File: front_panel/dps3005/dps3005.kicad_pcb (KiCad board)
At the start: 2 copper layers, 105.8 x 45.8 mm, 1 part

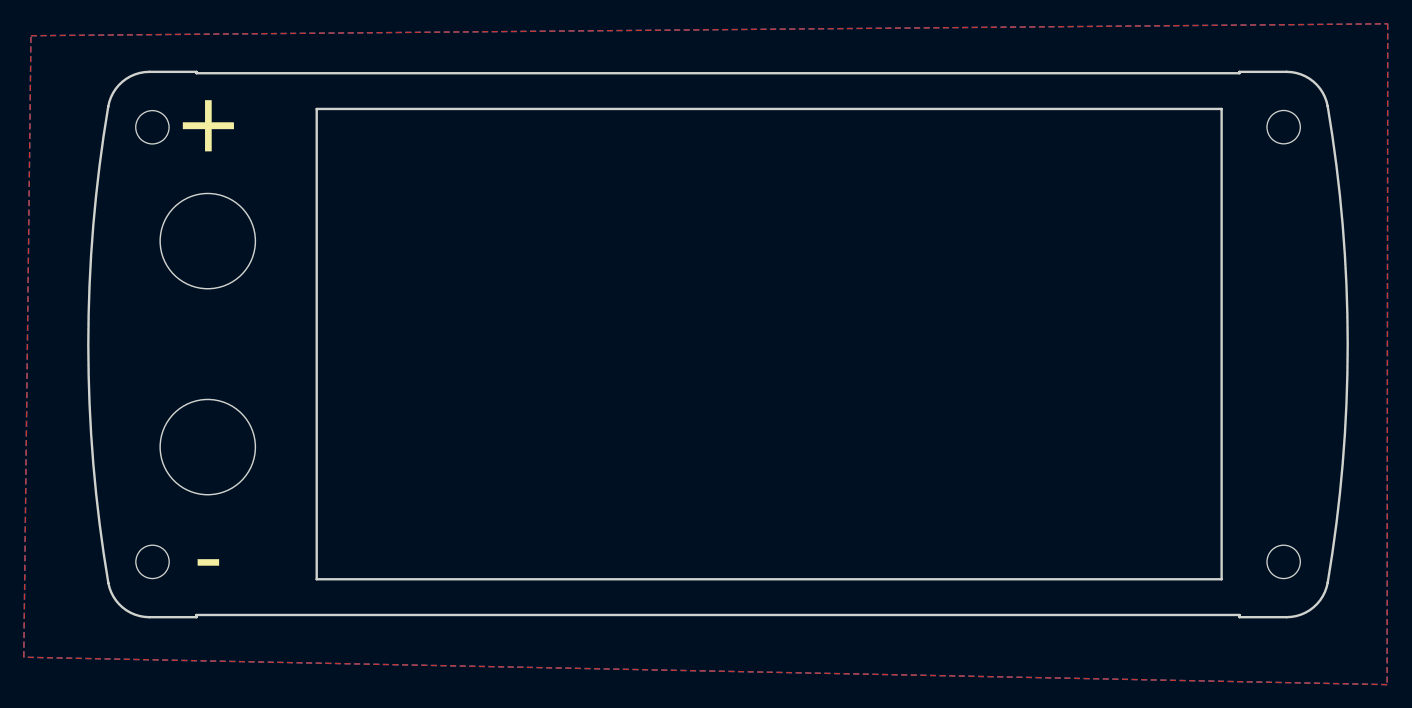
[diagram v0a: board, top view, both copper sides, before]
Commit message: Check failed again on JLCPCB because there was no drill file. All holes were made with the outline. Created a footprint for the binding posts and used KiCAD's 3mm mounting hole footprint for the screws. Sent back to JLCPCB for manufacture.
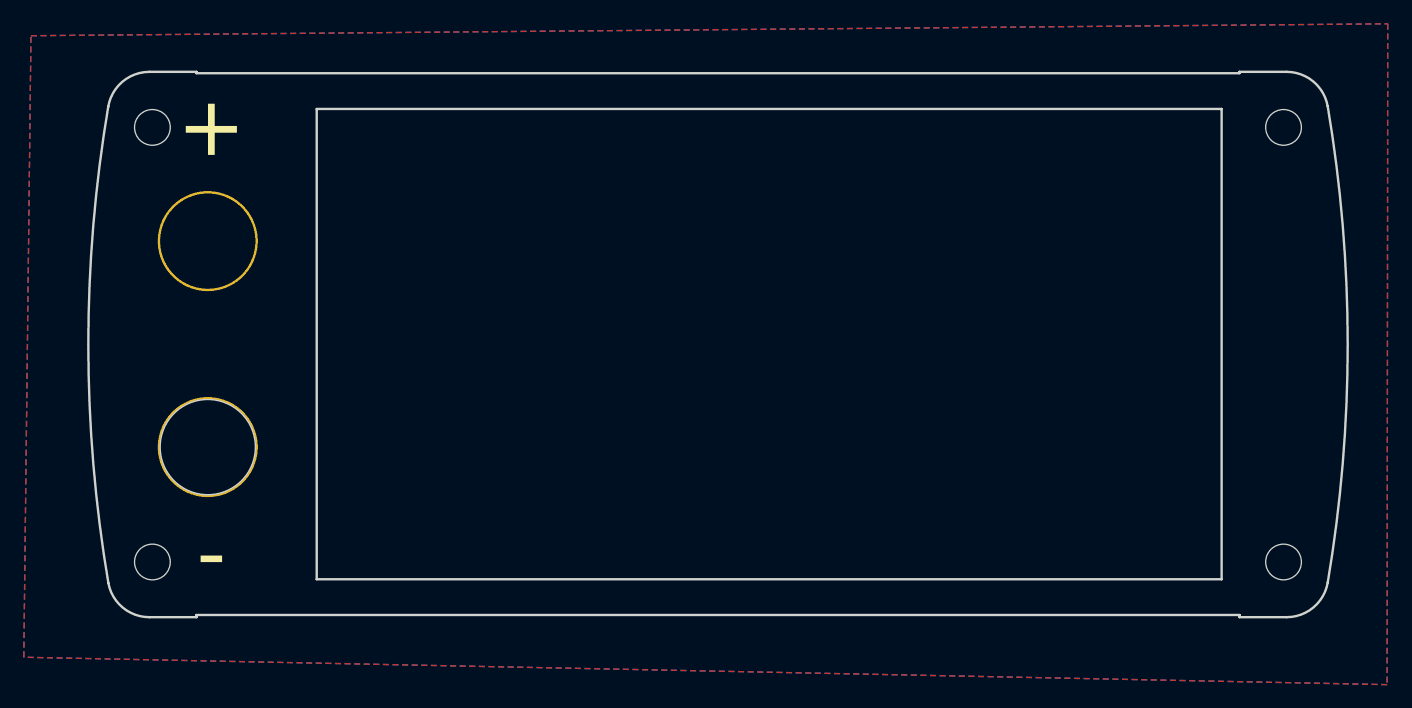
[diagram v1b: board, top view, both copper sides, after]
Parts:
- added REF**: BindingPost_8mm, front_panel:BindingPost_8mm, F.Cu at (81.5, 61.2)
- added REF**: BindingPost_8mm, front_panel:BindingPost_8mm, F.Cu at (81.5, 78.5)
- added REF**: MountingHole_3mm, MountingHole:MountingHole_3mm, F.Cu at (171.9, 51.6)
- added REF**: MountingHole_3mm, MountingHole:MountingHole_3mm, F.Cu at (171.9, 88.2)
- added REF**: MountingHole_3mm, MountingHole:MountingHole_3mm, F.Cu at (76.9, 88.2)
- added REF**: MountingHole_3mm, MountingHole:MountingHole_3mm, F.Cu at (76.9, 51.6)
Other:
- outline, holes or cut-outs redrawn
- rule pad_to_mask_clearance: 0.051 -> 0
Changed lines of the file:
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@@
   (general
     (thickness 1.6)
-    (drawings 2423)
+    (drawings 2416)
     (tracks 0)
     (zones 0)
-    (modules 1)
+    (modules 7)
     (nets 1)
   )
@@
     (mod_text_size 1 1)
     (mod_text_width 0.15)
-    (pad_size 1.524 1.524)
-    (pad_drill 0.762)
-    (pad_to_mask_clearance 0.051)
-    (solder_mask_min_width 0.25)
+    (pad_size 8.4 8.4)
+    (pad_drill 8)
+    (pad_to_mask_clearance 0)
     (aux_axis_origin 71.5 47)
     (grid_origin 71.5 47)
@@
     (uvia_dia 0.3)
     (uvia_drill 0.1)
+  )
+  (module front_panel:BindingPost_8mm (layer F.Cu)
+    (at 81.55 61.2)
+    (descr "BindingPost Hole 8mm drill 13mm diameter")
+    (tags "binding post")
+    (attr virtual)
+    (fp_text reference REF** (at 0 -5.2) (layer F.SilkS) hide
+      (effects (font (size 1 1) (thickness 0.15)))
+    )
+    (fp_text value BindingPost_8mm (at 13.3 0) (layer F.Fab) hide
+      (effects (font (size 1 1) (thickness 0.15)))
+    )
+    (fp_circle (center 0 0) (end 6.5 0) (layer F.CrtYd) (width 0.05))
+    (fp_text user %R (at 0.3 0) (layer F.Fab)
+      (effects (font (size 1 1) (thickness 0.15)))
+    )
+    (pad "" np_thru_hole circle (at 0 0) (size 8.4 8.4) (drill 8) (layers *.Cu *.Mask))
+  )
+  (module front_panel:BindingPost_8mm (layer F.Cu)
+    (at 81.55 78.5)
+    (descr "BindingPost Hole 8mm drill 13mm diameter")
+    (tags "binding post")
+    (attr virtual)
+    (fp_text reference REF** (at 0 -5.15) (layer F.SilkS) hide
+      (effects (font (size 1 1) (thickness 0.15)))
+    )
+    (fp_text value BindingPost_8mm (at 13.3 0.05) (layer F.Fab) hide
+      (effects (font (size 1 1) (thickness 0.15)))
+    )
+    (fp_circle (center 0 0) (end 6.5 0) (layer F.CrtYd) (width 0.05))
+    (fp_text user %R (at 0.3 0) (layer F.Fab)
+      (effects (font (size 1 1) (thickness 0.15)))
+    )
+    (pad "" np_thru_hole circle (at 0 0) (size 8.4 8.4) (drill 8) (layers *.Cu *.Mask))
+  )
+  (module MountingHole:MountingHole_3mm (layer F.Cu)
+    (at 171.9 51.65)
+    (descr "Mounting Hole 3mm, no annular")
+    (tags "mounting hole 3mm no annular")
+    (attr virtual)
+    (fp_text reference REF** (at 0 -4) (layer F.SilkS) hide
+      (effects (font (size 1 1) (thickness 0.15)))
+    )
+    (fp_text value MountingHole_3mm (at 0 4) (layer F.Fab)
+      (effects (font (size 1 1) (thickness 0.15)))
+    )
+    (fp_circle (center 0 0) (end 3.25 0) (layer F.CrtYd) (width 0.05))
+    (fp_circle (center 0 0) (end 3 0) (layer Cmts.User) (width 0.15))
+    (fp_text user %R (at 0.3 0) (layer F.Fab)
+      (effects (font (size 1 1) (thickness 0.15)))
+    )
+    (pad 1 np_thru_hole circle (at 0 0) (size 3 3) (drill 3) (layers *.Cu *.Mask))
+  )
+  (module MountingHole:MountingHole_3mm (layer F.Cu)
+    (at 171.9 88.15)
+    (descr "Mounting Hole 3mm, no annular")
+    (tags "mounting hole 3mm no annular")
+    (attr virtual)
+    (fp_text reference REF** (at 0 -4) (layer F.SilkS) hide
+      (effects (font (size 1 1) (thickness 0.15)))
+    )
+    (fp_text value MountingHole_3mm (at 0 4) (layer F.Fab)
+      (effects (font (size 1 1) (thickness 0.15)))
+    )
+    (fp_circle (center 0 0) (end 3.25 0) (layer F.CrtYd) (width 0.05))
+    (fp_circle (center 0 0) (end 3 0) (layer Cmts.User) (width 0.15))
+    (fp_text user %R (at 0.3 0) (layer F.Fab)
+      (effects (font (size 1 1) (thickness 0.15)))
+    )
+    (pad 1 np_thru_hole circle (at 0 0) (size 3 3) (drill 3) (layers *.Cu *.Mask))
+  )
+  (module MountingHole:MountingHole_3mm (layer F.Cu)
+    (at 76.9 88.15)
+    (descr "Mounting Hole 3mm, no annular")
+    (tags "mounting hole 3mm no annular")
+    (attr virtual)
+    (fp_text reference REF** (at 0 -4) (layer F.SilkS) hide
+      (effects (font (size 1 1) (thickness 0.15)))
+    )
+    (fp_text value MountingHole_3mm (at 0 4) (layer F.Fab)
+      (effects (font (size 1 1) (thickness 0.15)))
+    )
+    (fp_circle (center 0 0) (end 3.25 0) (layer F.CrtYd) (width 0.05))
+    (fp_circle (center 0 0) (end 3 0) (layer Cmts.User) (width 0.15))
+    (fp_text user %R (at 0.3 0) (layer F.Fab)
+      (effects (font (size 1 1) (thickness 0.15)))
+    )
+    (pad 1 np_thru_hole circle (at 0 0) (size 3 3) (drill 3) (layers *.Cu *.Mask))
+  )
+  (module MountingHole:MountingHole_3mm (layer F.Cu)
+    (at 76.9 51.65)
+    (descr "Mounting Hole 3mm, no annular")
+    (tags "mounting hole 3mm no annular")
+    (attr virtual)
+    (fp_text reference REF** (at 0 -4) (layer F.SilkS) hide
+      (effects (font (size 1 1) (thickness 0.15)))
+    )
+    (fp_text value MountingHole_3mm (at 0 4) (layer F.Fab)
+      (effects (font (size 1 1) (thickness 0.15)))
+    )
+    (fp_circle (center 0 0) (end 3.25 0) (layer F.CrtYd) (width 0.05))
+    (fp_circle (center 0 0) (end 3 0) (layer Cmts.User) (width 0.15))
+    (fp_text user %R (at 0.3 0) (layer F.Fab)
+      (effects (font (size 1 1) (thickness 0.15)))
+    )
+    (pad 1 np_thru_hole circle (at 0 0) (size 3 3) (drill 3) (layers *.Cu *.Mask))
   )
   (module front_panel:DPS3005 (layer F.Cu)
@@
     (arrow2b (pts (xy 71.5 44.75) (xy 72.626504 44.163579)))
   )
-  (gr_text - (at 81.6 51.35) (layer B.SilkS)
+  (gr_text - (at 81.85 51.65) (layer B.SilkS)
     (effects (font (size 5 5) (thickness 0.5)))
   )
-  (gr_text + (at 81.6 87.75) (layer B.SilkS)
+  (gr_text + (at 81.85 87.45) (layer B.SilkS)
     (effects (font (size 5 5) (thickness 0.5)))
   )
   (gr_line (start 71.5 70) (end 89.2 70) (layer Cmts.User) (width 0.15))
-  (gr_text - (at 81.6 87.75) (layer F.SilkS)
+  (gr_text - (at 81.85 87.45) (layer F.SilkS)
     (effects (font (size 5 5) (thickness 0.5)))
   )
-  (gr_circle (center 81.55 78.5) (end 88.35 78.5) (layer Dwgs.User) (width 0.15))
-  (gr_circle (center 81.55 61.2) (end 88.35 61.2) (layer Dwgs.User) (width 0.15))
-  (gr_text + (at 81.6 51.35) (layer F.SilkS)
+  (gr_text + (at 81.85 51.65) (layer F.SilkS)
     (effects (font (size 5 5) (thickness 0.5)))
   )
@@
   (gr_line (start 166.7 50.1) (end 166.7 89.6) (layer Edge.Cuts) (width 0.2))
   (gr_line (start 90.7 50.1) (end 166.7 50.1) (layer Edge.Cuts) (width 0.2))
-  (gr_circle (center 76.9 51.64) (end 78.3 51.64) (layer Edge.Cuts) (width 0.05))
-  (gr_circle (center 76.91 88.14) (end 78.31 88.14) (layer Edge.Cuts) (width 0.05))
-  (gr_circle (center 171.91 88.14) (end 173.31 88.14) (layer Edge.Cuts) (width 0.05))
-  (gr_circle (center 171.91 51.63) (end 173.31 51.63) (layer Edge.Cuts) (width 0.05))
   (gr_circle (center 81.55 78.5) (end 85.55 78.5) (layer Edge.Cuts) (width 0.12))
-  (gr_circle (center 81.55 61.2) (end 85.55 61.2) (layer Edge.Cuts) (width 0.12))
   (gr_arc (start 172.161319 50.484829) (end 175.606012 49.863932) (angle -79.77314564) (layer Edge.Cuts) (width 0.2))
   (gr_arc (start 76.644379 50.484829) (end 76.644379 46.984829) (angle -80.4) (layer Edge.Cuts) (width 0.2))
@@
     (connect_pads (clearance 0.2))
     (min_thickness 0.254)
-    (fill (arc_segments 32) (thermal_gap 0.508) (thermal_bridge_width 0.508))
+    (fill yes (arc_segments 32) (thermal_gap 0.508) (thermal_bridge_width 0.508))
     (polygon
       (pts
@@
     (connect_pads (clearance 0.2))
     (min_thickness 0.254)
-    (fill (arc_segments 32) (thermal_gap 0.508) (thermal_bridge_width 0.508))
+    (fill yes (arc_segments 32) (thermal_gap 0.508) (thermal_bridge_width 0.508))
     (polygon
       (pts
